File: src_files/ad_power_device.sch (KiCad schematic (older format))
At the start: 24 parts, among them J2 5622-6309-ML, J3 205957-0271, J7 Conn_01x05_Male, U11 NFC_VS1797SM

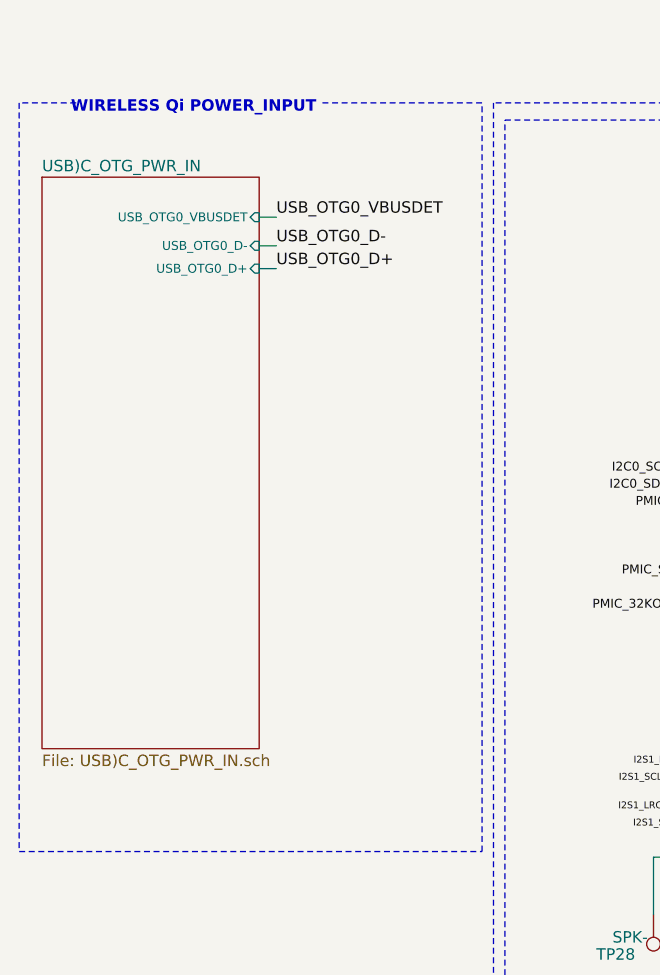
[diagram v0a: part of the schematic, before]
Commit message: updates rules check and associations
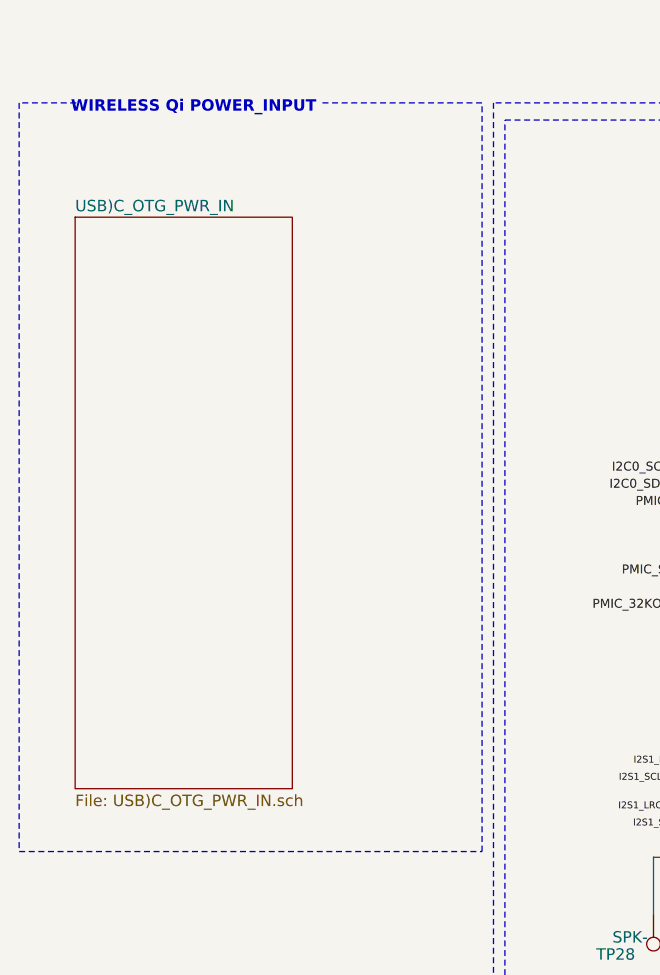
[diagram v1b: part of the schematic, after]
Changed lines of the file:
@@
 Wire Wire Line
 	8250 2625 8075 2625
-$Sheet
-S 625  875  950  2500
-U 6823D52E
-F0 "USB)C_OTG_PWR_IN" 50
-F1 "USB)C_OTG_PWR_IN.sch" 50
-F2 "USB_OTG0_VBUSDET" I R 1575 1050 39
-F3 "USB_OTG0_D-" I R 1575 1175 39
-F4 "USB_OTG0_D+" I R 1575 1275 39
-$EndSheet
-Text Label 1650 1275 0    50   ~ 0
-USB_OTG0_D+
-Text Label 1650 1175 0    50   ~ 0
-USB_OTG0_D-
-Text Label 1650 1050 0    50   ~ 0
-USB_OTG0_VBUSDET
-Wire Wire Line
-	1650 1275 1575 1275
-Wire Wire Line
-	1650 1175 1575 1175
-Wire Wire Line
-	1650 1050 1575 1050
 Text Notes 1825 600  2    50   ~ 10
 WIRELESS Qi POWER_INPUT
@@
 Wire Notes Line
 	15975 5675 14675 5675
+$Sheet
+S 770  1050 950  2500
+U 6823D52E
+F0 "USB)C_OTG_PWR_IN" 50
+F1 "USB)C_OTG_PWR_IN.sch" 50
+$EndSheet
 $EndSCHEMATC
